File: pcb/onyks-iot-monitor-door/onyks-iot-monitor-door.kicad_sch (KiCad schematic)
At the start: 17 parts, among them SW1 SW_Push, SW2 SW_Push, U1 ESP32-WROOM-32D, U2 SM353LT

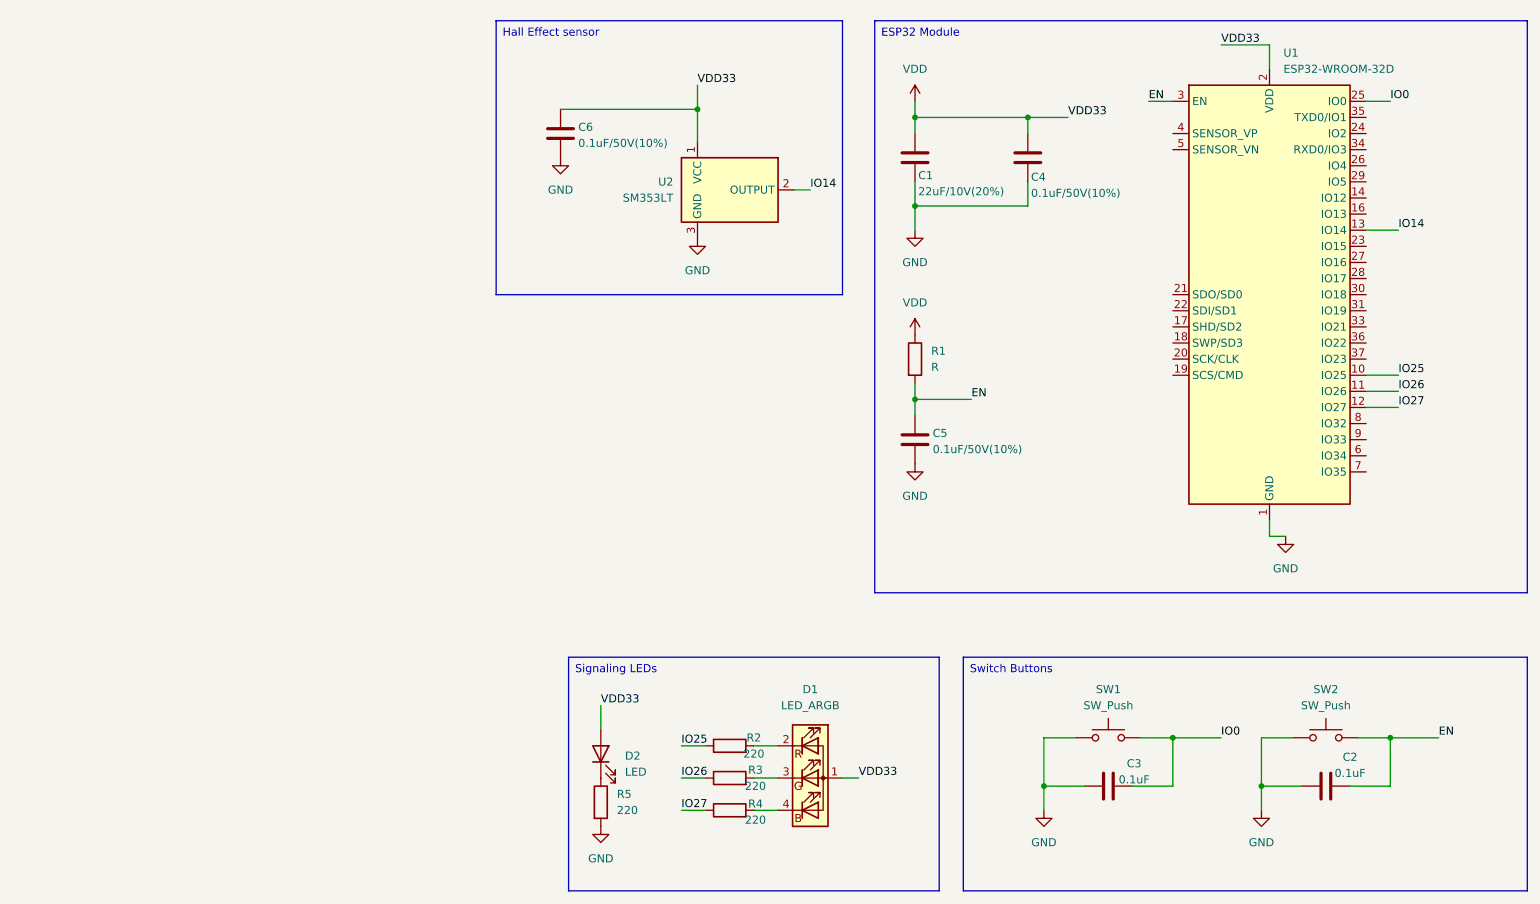
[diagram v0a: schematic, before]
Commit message: Finish schemat and pcb design (no GND)
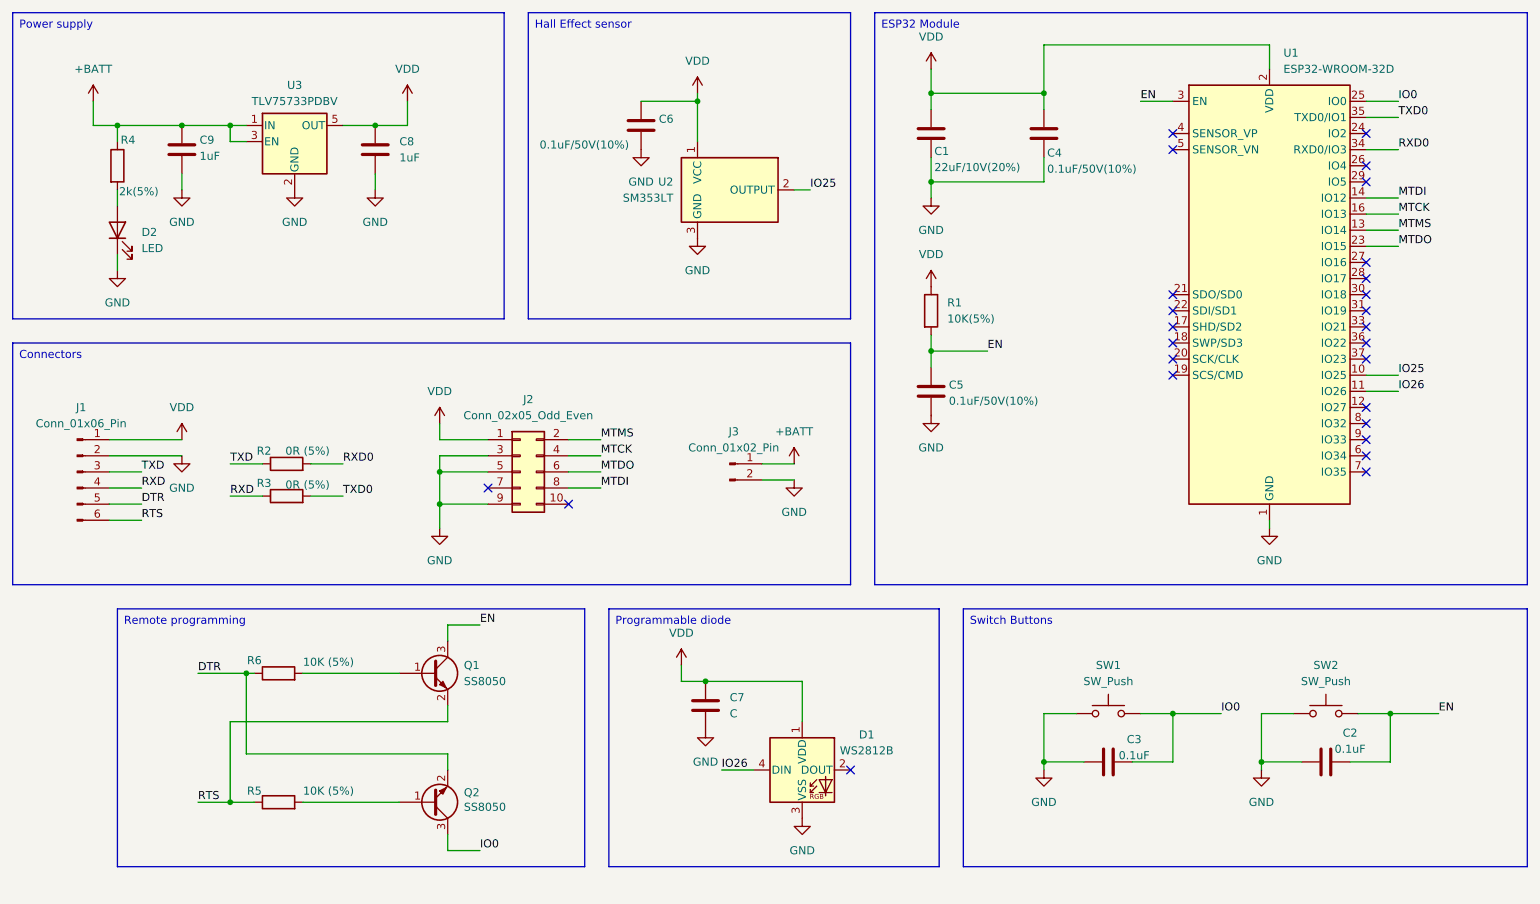
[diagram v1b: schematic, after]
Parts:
- removed D1: LED_ARGB, symbol Device:LED_ARGB
- added C7: C, Capacitor_SMD:C_0603_1608Metric, symbol Device:C
- added C8, C9: 1uF, Capacitor_SMD:C_0603_1608Metric, symbol Device:C
- added D1: WS2812B, LED_SMD:LED_WS2812B_PLCC4_5.0x5.0mm_P3.2mm, symbol LED:WS2812B
- added J1: Conn_01x06_Pin, Connector_PinHeader_2.54mm:PinHeader_1x06_P2.54mm_Vertical, symbol Connector:Conn_01x06_Pin
- added J2: Conn_02x05_Odd_Even, Connector_PinHeader_2.54mm:PinHeader_2x05_P2.54mm_Vertical, symbol Connector_Generic:Conn_02x05_Odd_Even
- added J3: Conn_01x02_Pin, Connector_PinHeader_2.54mm:PinHeader_1x02_P2.54mm_Vertical, symbol Connector:Conn_01x02_Pin
- added Q1, Q2: SS8050, Package_TO_SOT_SMD:SOT-23, symbol Transistor_BJT:SS8050
- added R6: 10K (5%), Resistor_SMD:R_0603_1608Metric, symbol Device:R
- added U3: TLV75733PDBV, Package_TO_SOT_SMD:SOT-23-5, symbol Regulator_Linear:TLV75733PDBV
- C1, C2, C3, C4, C5, C6: footprint (none) -> Capacitor_SMD:C_0603_1608Metric
- D2: footprint (none) -> LED_SMD:LED_0201_0603Metric
- R1: value R -> 10K(5%); footprint (none) -> Resistor_SMD:R_0603_1608Metric
- R2, R3: value 220 -> 0R (5%); footprint (none) -> Resistor_SMD:R_0603_1608Metric
- R4: value 220 -> 2k(5%); footprint (none) -> Resistor_SMD:R_0603_1608Metric
- R5: value 220 -> 10K (5%); footprint (none) -> Resistor_SMD:R_0603_1608Metric
- SW1, SW2: footprint (none) -> Button_Switch_SMD:SW_Tactile_SPST_NO_Straight_CK_PTS636Sx25SMTRLFS
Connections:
- net EN: now also Q1.3 (C)
- net GND: now also D2.1 (K), C7.2, C8.2, C9.2, D1.3 (VSS), J1.2 (Pin_2), J2.3 (Pin_3), J2.5 (Pin_5), J2.9 (Pin_9), J3.2 (Pin_2), U3.2 (GND); no longer R5.2
- net IO0: now also Q2.3 (C)
- net IO25: now also U2.2 (OUTPUT); no longer R2.1
- net IO26: now also D1.4 (DIN); no longer R3.1
- net VDD: now also C7.1, C8.1, D1.1 (VDD), J1.1 (Pin_1), J2.1 (Pin_1), U3.5 (OUT); no longer D2.2 (A)
- net RXD0: now reaches R2.2
- net RXD0: now also U1.34 (RXD0/IO3)
- net TXD0: now reaches R3.2
- net TXD0: now also U1.35 (TXD0/IO1)
- net at R4.2: now also D2.2 (A)
- net RTS: now reaches R5.1
- net RTS: now also J1.6 (Pin_6), Q1.2 (E); no longer D2.1 (K)
- net MTDI: now reaches U1.14 (IO12)
- net MTDI: now also J2.8 (Pin_8)
- net MTCK: now reaches U1.16 (IO13)
- net MTCK: now also J2.4 (Pin_4)
- net MTDO: now reaches U1.23 (IO15)
- net MTDO: now also J2.6 (Pin_6)
- net IO14 renamed MTMS
- net MTMS: now also J2.2 (Pin_2); no longer U2.2 (OUTPUT)
- net IO27: no longer names the net of U1.12 (IO27)
- net IO27: no longer R4.1
- new net: Q1.1 (B), R6.2
- new net: Q2.1 (B), R5.2
- new net +BATT: C9.1, J3.1 (Pin_1), R4.1, U3.1 (IN), U3.3 (EN)
- new net DTR: J1.5 (Pin_5), Q2.2 (E), R6.1
- new net RXD: J1.4 (Pin_4), R3.1
- new net TXD: J1.3 (Pin_3), R2.1
- no-connect marks 0 -> 26
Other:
- moved on the sheet: C1, C2, C3, C4, C5, C6, R1, SW1, SW2
